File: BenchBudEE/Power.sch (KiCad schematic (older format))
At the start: 0 parts

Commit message: Power module blocked out + added power adjustment monitor module
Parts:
- added C? (x2): C, ~, symbol C
- added F? (x4): FUSE, ~, symbol FUSE
- added L? (x2): INDUCTOR, ~, symbol INDUCTOR
- added P?: CONN_12X2, symbol CONN_12X2
- added R?: R, ~, symbol R
- added SW?: SWITCH_INV, ~, symbol SWITCH_INV
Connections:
- new net: F?.1, P?.10 (P10)
- new net: F?.1, P?.14 (P14)
- new net: P?.16 (P16), SW?.2
- new net: F?.1, P?.2 (P2)
- new net: F?.1, P?.4 (P4), P?.6 (P6)
- new net: R?.1, SW?.1
- new net +12P: C?.1, F?.2, L?.1, L?.2
- new net +3.3V: F?.2, R?.2
- new net +5V: F?.2
- new net -12P: C?.2, F?.2, L?.1, L?.2
- new net GND: C?.1, C?.2, P?.3 (P3), P?.5 (P5), SW?.3

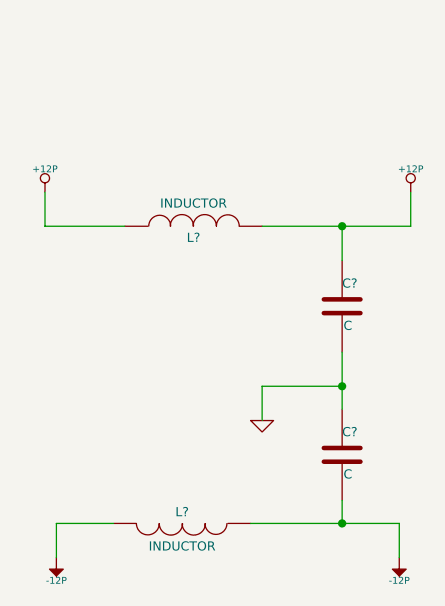
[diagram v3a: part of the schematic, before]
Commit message: Power monitor module blocked out (needs tidying)
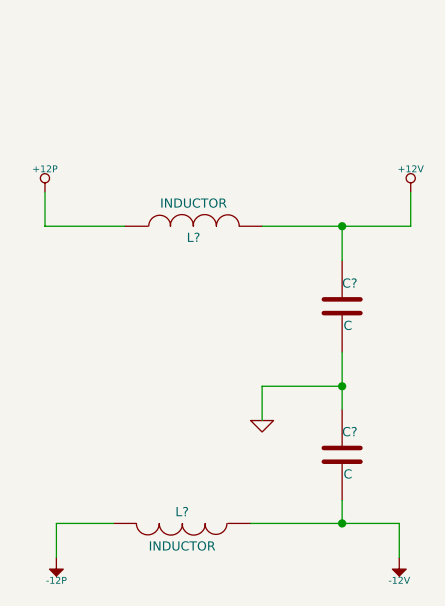
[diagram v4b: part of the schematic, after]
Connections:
- net +12P: no longer C?.1, L?.2
- net -12P: no longer C?.2, L?.1
- new net +12V: C?.1, L?.2
- new net -12V: C?.2, L?.1
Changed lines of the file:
@@
 Sheet 6 9
 Title ""
-Date "5 feb 2014"
+Date "6 feb 2014"
 Rev ""
 Comp ""
@@
 	9700 3350 10050 3350
 Connection ~ 10050 3350
-$Comp
-L +12P #PWR?
-U 1 1 52F2E05F
-P 10350 2500
-F 0 "#PWR?" H 10350 2470 30  0001 C CNN
-F 1 "+12P" H 10350 2600 30  0000 C CNN
-F 2 "" H 10350 2500 60  0000 C CNN
-F 3 "" H 10350 2500 60  0000 C CNN
-	1    10350 2500
-	1    0    0    -1
-$EndComp
 Wire Wire Line
 	8750 2500 8750 2650
 Wire Wire Line
 	8750 2650 9100 2650
-Wire Wire Line
-	10350 2650 10350 2500
 Connection ~ 10050 2650
 Wire Wire Line
@@
 Wire Wire Line
 	8800 3950 8800 4100
-$Comp
-L -12P #PWR?
-U 1 1 52F2E0F8
+Connection ~ 10050 3950
+$Comp
+L -12V #PWR?
+U 1 1 52F3102F
 P 10300 4100
 F 0 "#PWR?" H 10300 4230 20  0001 C CNN
-F 1 "-12P" H 10300 4200 30  0000 C CNN
+F 1 "-12V" H 10300 4200 30  0000 C CNN
 F 2 "" H 10300 4100 60  0000 C CNN
 F 3 "" H 10300 4100 60  0000 C CNN
@@
 Wire Wire Line
 	10300 3950 10300 4100
-Connection ~ 10050 3950
+$Comp
+L +12V #PWR?
+U 1 1 52F31097
+P 10350 2500
+F 0 "#PWR?" H 10350 2450 20  0001 C CNN
+F 1 "+12V" H 10350 2600 30  0000 C CNN
+F 2 "" H 10350 2500 60  0000 C CNN
+F 3 "" H 10350 2500 60  0000 C CNN
+	1    10350 2500
+	1    0    0    -1
+$EndComp
+Wire Wire Line
+	10350 2650 10350 2500
 $EndSCHEMATC

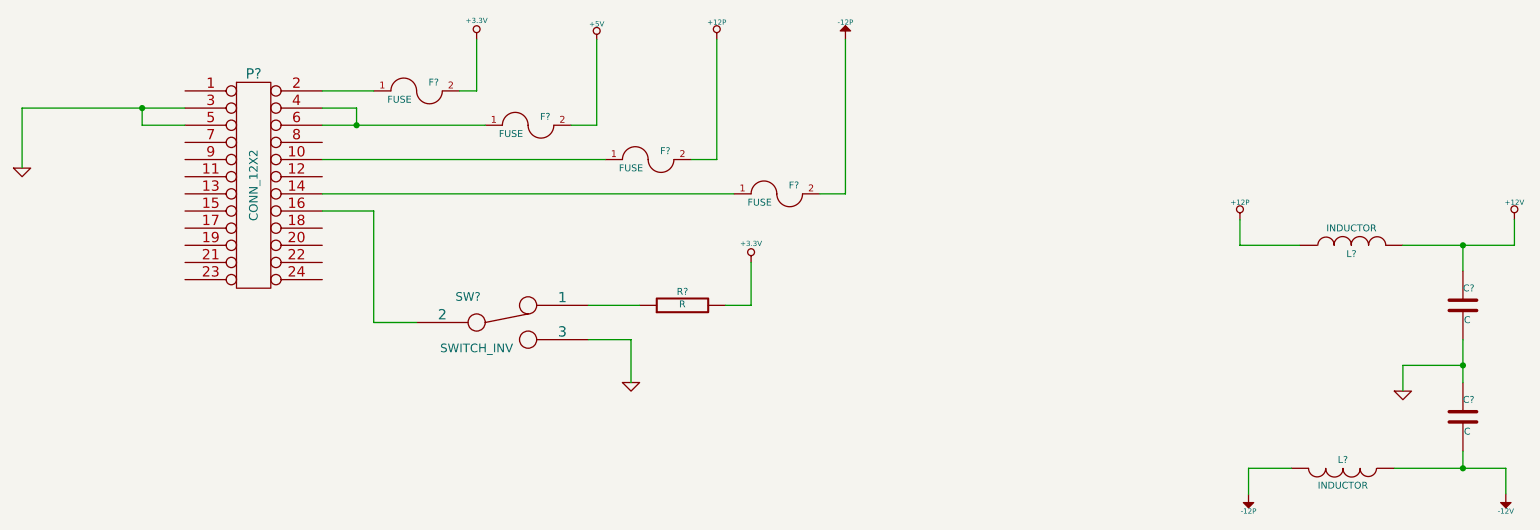
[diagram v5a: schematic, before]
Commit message: Parts added to relay module. Schematic tidied up.
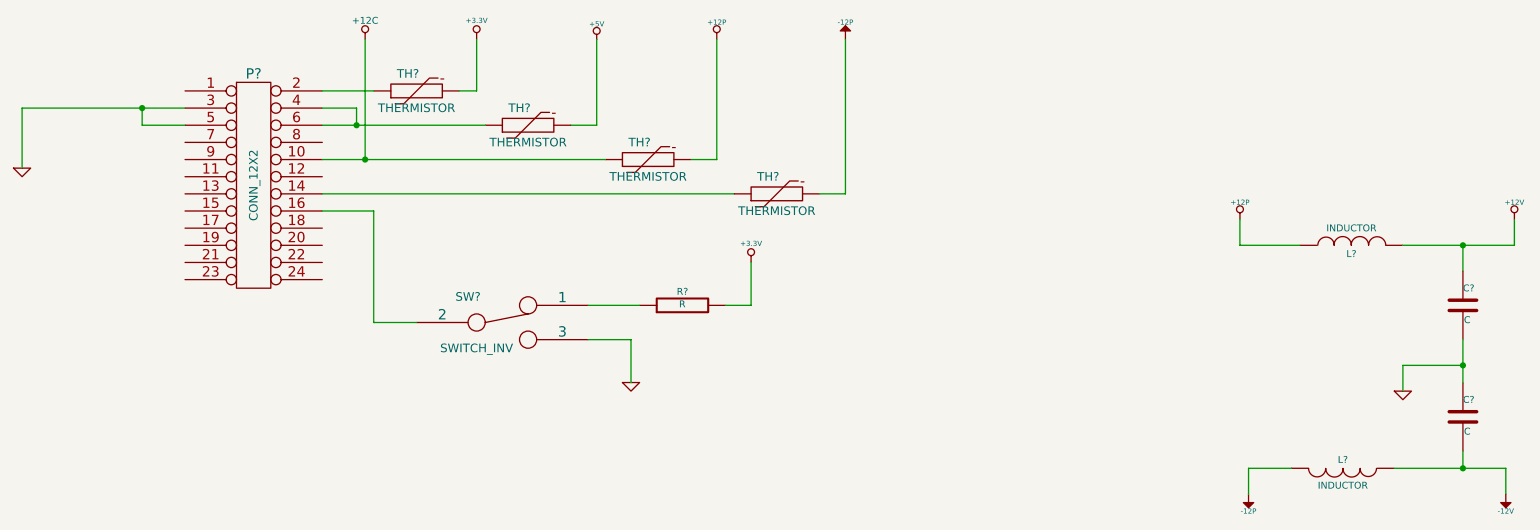
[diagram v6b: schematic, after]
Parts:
- removed F? (x4): FUSE, ~, symbol FUSE
- added TH? (x4): THERMISTOR, ~, symbol THERMISTOR
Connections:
- net +12P: now also TH?.2
- net +3.3V: now also TH?.2
- net +5V: now also TH?.2
- net -12P: now also TH?.2
- net +12C: now reaches P?.10 (P10)
- net +12C: now also TH?.1
- net at P?.14 (P14): now also TH?.1
- net at P?.2 (P2): now also TH?.1
- net at P?.4 (P4), P?.6 (P6): now also TH?.1
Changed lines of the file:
@@
 Sheet 5 9
 Title ""
-Date "8 feb 2014"
+Date "19 feb 2014"
 Rev ""
 Comp ""
@@
 $EndComp
 $Comp
-L FUSE F?
-U 1 1 52F2DB79
-P 3950 1750
-F 0 "F?" H 4050 1800 40  0000 C CNN
-F 1 "FUSE" H 3850 1700 40  0000 C CNN
-F 2 "~" H 3950 1750 60  0000 C CNN
-F 3 "~" H 3950 1750 60  0000 C CNN
-	1    3950 1750
-	1    0    0    -1
-$EndComp
-$Comp
-L FUSE F?
-U 1 1 52F2DB86
-P 4600 1950
-F 0 "F?" H 4700 2000 40  0000 C CNN
-F 1 "FUSE" H 4500 1900 40  0000 C CNN
-F 2 "~" H 4600 1950 60  0000 C CNN
-F 3 "~" H 4600 1950 60  0000 C CNN
-	1    4600 1950
-	1    0    0    -1
-$EndComp
-$Comp
-L FUSE F?
-U 1 1 52F2DB8C
-P 6050 2350
-F 0 "F?" H 6150 2400 40  0000 C CNN
-F 1 "FUSE" H 5950 2300 40  0000 C CNN
-F 2 "~" H 6050 2350 60  0000 C CNN
-F 3 "~" H 6050 2350 60  0000 C CNN
-	1    6050 2350
-	1    0    0    -1
-$EndComp
-$Comp
-L FUSE F?
-U 1 1 52F2DB92
-P 5300 2150
-F 0 "F?" H 5400 2200 40  0000 C CNN
-F 1 "FUSE" H 5200 2100 40  0000 C CNN
-F 2 "~" H 5300 2150 60  0000 C CNN
-F 3 "~" H 5300 2150 60  0000 C CNN
-	1    5300 2150
-	1    0    0    -1
-$EndComp
-$Comp
 L SWITCH_INV SW?
 U 1 1 52F2DBB8
@@
 	1    0    0    -1
 $EndComp
-Wire Wire Line
-	3400 1750 3700 1750
-Wire Wire Line
-	4200 1750 4300 1750
-Wire Wire Line
-	4300 1750 4300 1450
-Wire Wire Line
-	3400 1950 4350 1950
 Connection ~ 3600 1950
 Wire Wire Line
-	4850 1950 5000 1950
-Wire Wire Line
 	5000 1950 5000 1450
 Wire Wire Line
 	5800 2350 3400 2350
-Wire Wire Line
-	3400 2150 5050 2150
 Wire Wire Line
 	3600 1950 3600 1850
@@
 	6450 2350 6450 1450
 Wire Wire Line
-	2600 1850 1650 1850
+	2600 1850 2350 1850
+Wire Wire Line
+	2350 1850 1650 1850
 Wire Wire Line
 	2600 1950 2350 1950
@@
 $EndComp
 Wire Wire Line
-	9700 2650 10350 2650
+	9700 2650 10050 2650
+Wire Wire Line
+	10050 2650 10350 2650
 Wire Wire Line
 	10050 2650 10050 2800
 Wire Wire Line
-	10050 3200 10050 3450
-Wire Wire Line
-	9650 3950 10300 3950
+	10050 3200 10050 3350
+Wire Wire Line
+	10050 3350 10050 3450
+Wire Wire Line
+	9650 3950 10050 3950
+Wire Wire Line
+	10050 3950 10300 3950
 Wire Wire Line
 	10050 3950 10050 3850
@@
 Wire Wire Line
 	10350 2650 10350 2500
+Connection ~ 3650 2150
+$Comp
+L +12C #PWR?
+U 1 1 52F7EF09
+P 3650 1450
+F 0 "#PWR?" H 3650 1420 30  0001 C CNN
+F 1 "+12C" H 3650 1560 40  0000 C CNN
+F 2 "" H 3650 1450 60  0000 C CNN
+F 3 "" H 3650 1450 60  0000 C CNN
+	1    3650 1450
+	1    0    0    -1
+$EndComp
+Wire Wire Line
+	3650 1450 3650 2150
+$Comp
+L THERMISTOR TH?
+U 1 1 52F7EF46
+P 3950 1750
+F 0 "TH?" V 4050 1800 50  0000 C CNN
+F 1 "THERMISTOR" V 3850 1750 50  0000 C CNN
+F 2 "~" H 3950 1750 60  0000 C CNN
+F 3 "~" H 3950 1750 60  0000 C CNN
+	1    3950 1750
+	0    -1   -1   0
+$EndComp
+$Comp
+L THERMISTOR TH?
+U 1 1 52F7EF53
+P 4600 1950
+F 0 "TH?" V 4700 2000 50  0000 C CNN
+F 1 "THERMISTOR" V 4500 1950 50  0000 C CNN
+F 2 "~" H 4600 1950 60  0000 C CNN
+F 3 "~" H 4600 1950 60  0000 C CNN
+	1    4600 1950
+	0    -1   -1   0
+$EndComp
+$Comp
+L THERMISTOR TH?
+U 1 1 52F7EF59
+P 5300 2150
+F 0 "TH?" V 5400 2200 50  0000 C CNN
+F 1 "THERMISTOR" V 5200 2150 50  0000 C CNN
+F 2 "~" H 5300 2150 60  0000 C CNN
+F 3 "~" H 5300 2150 60  0000 C CNN
+	1    5300 2150
+	0    -1   -1   0
+$EndComp
+$Comp
+L THERMISTOR TH?
+U 1 1 52F7EF5F
+P 6050 2350
+F 0 "TH?" V 6150 2400 50  0000 C CNN
+F 1 "THERMISTOR" V 5950 2350 50  0000 C CNN
+F 2 "~" H 6050 2350 60  0000 C CNN
+F 3 "~" H 6050 2350 60  0000 C CNN
+	1    6050 2350
+	0    -1   -1   0
+$EndComp
+Wire Wire Line
+	3400 1750 3700 1750
+Wire Wire Line
+	4200 1750 4300 1750
+Wire Wire Line
+	4300 1750 4300 1450
+Wire Wire Line
+	3400 1950 3600 1950
+Wire Wire Line
+	3600 1950 4350 1950
+Wire Wire Line
+	4850 1950 5000 1950
+Wire Wire Line
+	3400 2150 3650 2150
+Wire Wire Line
+	3650 2150 5050 2150
 $EndSCHEMATC

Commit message: Design rules specified for layout.
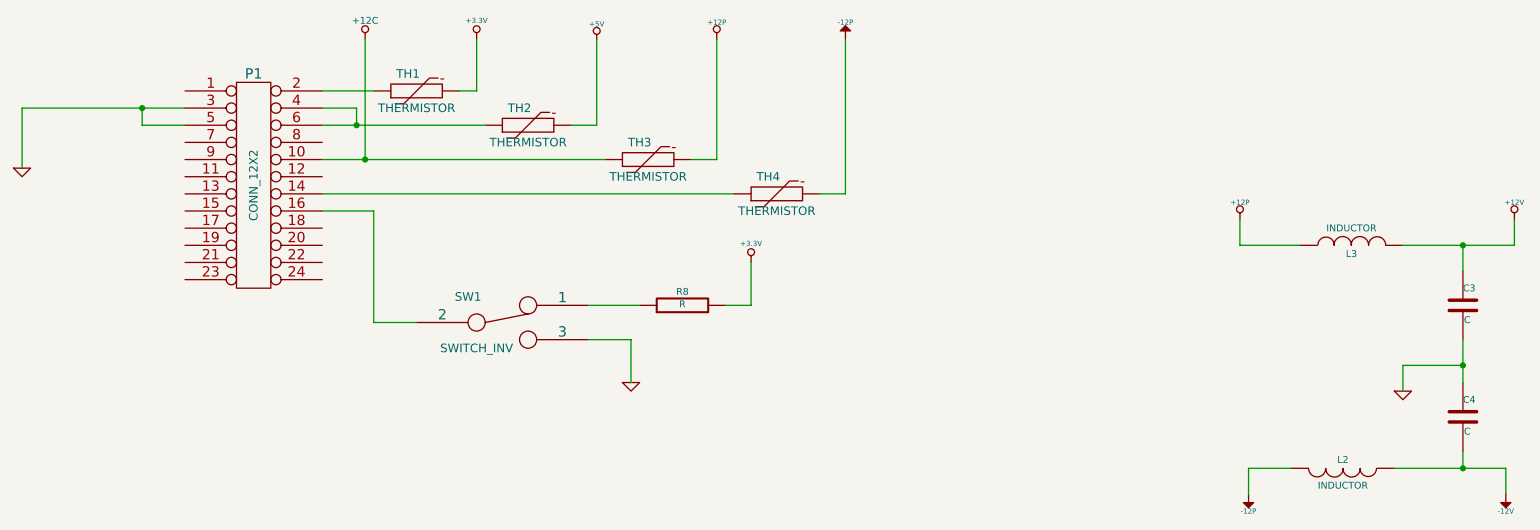
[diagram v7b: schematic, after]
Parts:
- gave numbers to parts that had none: 11
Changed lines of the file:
@@
 $EndDescr
 $Comp
-L CONN_12X2 P?
+L CONN_12X2 P1
 U 1 1 52F2DAD0
 P 3000 2300
-F 0 "P?" H 3000 2950 60  0000 C CNN
+F 0 "P1" H 3000 2950 60  0000 C CNN
 F 1 "CONN_12X2" V 3000 2300 50  0000 C CNN
 F 2 "" H 3000 2300 60  0000 C CNN
@@
 	1650 1850 1650 2200
 $Comp
-L GND #PWR?
+L GND #PWR10
 U 1 1 52F2DAF8
 P 1650 2200
-F 0 "#PWR?" H 1650 2200 30  0001 C CNN
+F 0 "#PWR10" H 1650 2200 30  0001 C CNN
 F 1 "GND" H 1650 2130 30  0001 C CNN
 F 2 "" H 1650 2200 60  0000 C CNN
@@
 $EndComp
 $Comp
-L +3.3V #PWR?
+L +3.3V #PWR12
 U 1 1 52F2DB2F
 P 4300 1450
-F 0 "#PWR?" H 4300 1410 30  0001 C CNN
+F 0 "#PWR12" H 4300 1410 30  0001 C CNN
 F 1 "+3.3V" H 4300 1560 30  0000 C CNN
 F 2 "" H 4300 1450 60  0000 C CNN
@@
 $EndComp
 $Comp
-L +5V #PWR?
+L +5V #PWR13
 U 1 1 52F2DB50
 P 5000 1450
-F 0 "#PWR?" H 5000 1540 20  0001 C CNN
+F 0 "#PWR13" H 5000 1540 20  0001 C CNN
 F 1 "+5V" H 5000 1540 30  0000 C CNN
 F 2 "" H 5000 1450 60  0000 C CNN
@@
 $EndComp
 $Comp
-L SWITCH_INV SW?
+L SWITCH_INV SW1
 U 1 1 52F2DBB8
 P 4450 3100
-F 0 "SW?" H 4250 3250 50  0000 C CNN
+F 0 "SW1" H 4250 3250 50  0000 C CNN
 F 1 "SWITCH_INV" H 4300 2950 50  0000 C CNN
 F 2 "~" H 4450 3100 60  0000 C CNN
@@
 	3600 1850 3400 1850
 $Comp
-L +12P #PWR?
+L +12P #PWR15
 U 1 1 52F2DC76
 P 5700 1450
-F 0 "#PWR?" H 5700 1420 30  0001 C CNN
+F 0 "#PWR15" H 5700 1420 30  0001 C CNN
 F 1 "+12P" H 5700 1550 30  0000 C CNN
 F 2 "" H 5700 1450 60  0000 C CNN
@@
 	5700 2150 5700 1450
 $Comp
-L -12P #PWR?
+L -12P #PWR17
 U 1 1 52F2DCDB
 P 6450 1450
-F 0 "#PWR?" H 6450 1580 20  0001 C CNN
+F 0 "#PWR17" H 6450 1580 20  0001 C CNN
 F 1 "-12P" H 6450 1550 30  0000 C CNN
 F 2 "" H 6450 1450 60  0000 C CNN
@@
 	3700 3100 3950 3100
 $Comp
-L GND #PWR?
+L GND #PWR14
 U 1 1 52F2DD3B
 P 5200 3450
-F 0 "#PWR?" H 5200 3450 30  0001 C CNN
+F 0 "#PWR14" H 5200 3450 30  0001 C CNN
 F 1 "GND" H 5200 3380 30  0001 C CNN
 F 2 "" H 5200 3450 60  0000 C CNN
@@
 	5200 3200 5200 3450
 $Comp
-L R R?
+L R R8
 U 1 1 52F2DD5B
 P 5500 3000
-F 0 "R?" V 5580 3000 40  0000 C CNN
+F 0 "R8" V 5580 3000 40  0000 C CNN
 F 1 "R" V 5507 3001 40  0000 C CNN
 F 2 "~" V 5430 3000 30  0000 C CNN
@@
 $EndComp
 $Comp
-L +3.3V #PWR?
+L +3.3V #PWR16
 U 1 1 52F2DD68
 P 5900 2750
-F 0 "#PWR?" H 5900 2710 30  0001 C CNN
+F 0 "#PWR16" H 5900 2710 30  0001 C CNN
 F 1 "+3.3V" H 5900 2860 30  0000 C CNN
 F 2 "" H 5900 2750 60  0000 C CNN
@@
 	5900 3000 5900 2750
 $Comp
-L +12P #PWR?
+L +12P #PWR18
 U 1 1 52F2DF60
 P 8750 2500
-F 0 "#PWR?" H 8750 2470 30  0001 C CNN
+F 0 "#PWR18" H 8750 2470 30  0001 C CNN
 F 1 "+12P" H 8750 2600 30  0000 C CNN
 F 2 "" H 8750 2500 60  0000 C CNN
@@
 $EndComp
 $Comp
-L -12P #PWR?
+L -12P #PWR19
 U 1 1 52F2DF66
 P 8800 4100
-F 0 "#PWR?" H 8800 4230 20  0001 C CNN
+F 0 "#PWR19" H 8800 4230 20  0001 C CNN
 F 1 "-12P" H 8800 4200 30  0000 C CNN
 F 2 "" H 8800 4100 60  0000 C CNN
@@
 $EndComp
 $Comp
-L GND #PWR?
+L GND #PWR20
 U 1 1 52F2DF6C
 P 9700 3500
-F 0 "#PWR?" H 9700 3500 30  0001 C CNN
+F 0 "#PWR20" H 9700 3500 30  0001 C CNN
 F 1 "GND" H 9700 3430 30  0001 C CNN
 F 2 "" H 9700 3500 60  0000 C CNN
@@
 $EndComp
 $Comp
-L INDUCTOR L?
+L INDUCTOR L2
 U 1 1 52F2DF91
 P 9350 3950
-F 0 "L?" V 9300 3950 40  0000 C CNN
+F 0 "L2" V 9300 3950 40  0000 C CNN
 F 1 "INDUCTOR" V 9450 3950 40  0000 C CNN
 F 2 "~" H 9350 3950 60  0000 C CNN
@@
 $EndComp
 $Comp
-L C C?
+L C C3
 U 1 1 52F2DFA0
 P 10050 3000
-F 0 "C?" H 10050 3100 40  0000 L CNN
+F 0 "C3" H 10050 3100 40  0000 L CNN
 F 1 "C" H 10056 2915 40  0000 L CNN
 F 2 "~" H 10088 2850 30  0000 C CNN
@@
 $EndComp
 $Comp
-L INDUCTOR L?
+L INDUCTOR L3
 U 1 1 52F2DFAD
 P 9400 2650
-F 0 "L?" V 9350 2650 40  0000 C CNN
+F 0 "L3" V 9350 2650 40  0000 C CNN
 F 1 "INDUCTOR" V 9500 2650 40  0000 C CNN
 F 2 "~" H 9400 2650 60  0000 C CNN
@@
 $EndComp
 $Comp
-L C C?
+L C C4
 U 1 1 52F2DFD1
 P 10050 3650
-F 0 "C?" H 10050 3750 40  0000 L CNN
+F 0 "C4" H 10050 3750 40  0000 L CNN
 F 1 "C" H 10056 3565 40  0000 L CNN
 F 2 "~" H 10088 3500 30  0000 C CNN
@@
 Connection ~ 10050 3950
 $Comp
-L -12V #PWR?
+L -12V #PWR21
 U 1 1 52F3102F
 P 10300 4100
-F 0 "#PWR?" H 10300 4230 20  0001 C CNN
+F 0 "#PWR21" H 10300 4230 20  0001 C CNN
 F 1 "-12V" H 10300 4200 30  0000 C CNN
 F 2 "" H 10300 4100 60  0000 C CNN
@@
 	10300 3950 10300 4100
 $Comp
-L +12V #PWR?
+L +12V #PWR22
 U 1 1 52F31097
 P 10350 2500
-F 0 "#PWR?" H 10350 2450 20  0001 C CNN
+F 0 "#PWR22" H 10350 2450 20  0001 C CNN
 F 1 "+12V" H 10350 2600 30  0000 C CNN
 F 2 "" H 10350 2500 60  0000 C CNN
@@
 Connection ~ 3650 2150
 $Comp
-L +12C #PWR?
+L +12C #PWR11
 U 1 1 52F7EF09
 P 3650 1450
-F 0 "#PWR?" H 3650 1420 30  0001 C CNN
+F 0 "#PWR11" H 3650 1420 30  0001 C CNN
 F 1 "+12C" H 3650 1560 40  0000 C CNN
 F 2 "" H 3650 1450 60  0000 C CNN
@@
 	3650 1450 3650 2150
 $Comp
-L THERMISTOR TH?
+L THERMISTOR TH1
 U 1 1 52F7EF46
 P 3950 1750
-F 0 "TH?" V 4050 1800 50  0000 C CNN
+F 0 "TH1" V 4050 1800 50  0000 C CNN
 F 1 "THERMISTOR" V 3850 1750 50  0000 C CNN
 F 2 "~" H 3950 1750 60  0000 C CNN
@@
 $EndComp
 $Comp
-L THERMISTOR TH?
+L THERMISTOR TH2
 U 1 1 52F7EF53
 P 4600 1950
-F 0 "TH?" V 4700 2000 50  0000 C CNN
+F 0 "TH2" V 4700 2000 50  0000 C CNN
 F 1 "THERMISTOR" V 4500 1950 50  0000 C CNN
 F 2 "~" H 4600 1950 60  0000 C CNN
@@
 $EndComp
 $Comp
-L THERMISTOR TH?
+L THERMISTOR TH3
 U 1 1 52F7EF59
 P 5300 2150
-F 0 "TH?" V 5400 2200 50  0000 C CNN
+F 0 "TH3" V 5400 2200 50  0000 C CNN
 F 1 "THERMISTOR" V 5200 2150 50  0000 C CNN
 F 2 "~" H 5300 2150 60  0000 C CNN
@@
 $EndComp
 $Comp
-L THERMISTOR TH?
+L THERMISTOR TH4
 U 1 1 52F7EF5F
 P 6050 2350
-F 0 "TH?" V 6150 2400 50  0000 C CNN
+F 0 "TH4" V 6150 2400 50  0000 C CNN
 F 1 "THERMISTOR" V 5950 2350 50  0000 C CNN
 F 2 "~" H 6050 2350 60  0000 C CNN
